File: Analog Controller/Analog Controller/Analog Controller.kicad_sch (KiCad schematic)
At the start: 12 parts, among them J1 Conn_02x06_Odd_Even, J2 Conn_02x06_Odd_Even

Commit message: Completed Analog Controller Board
Completed Analog Controller Board schematic and pcb layout :)
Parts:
- removed J1, J2: Conn_02x06_Odd_Even, symbol Connector_Generic:Conn_02x06_Odd_Even
- added C10, C11, C12, C13, C14, C15, C16, C17, C18, C4, C5, C6, C7, C8, C9: 100n, Resistor_SMD:R_0603_1608Metric_Pad0.98x0.95mm_HandSolder, symbol Device:C_Small
- added D3, D4, D5: G, LED_SMD:LED_0603_1608Metric_Pad1.05x0.95mm_HandSolder, symbol Device:LED
- added H1, H2, H3, H4: No. 8, MountingHole:MountingHole_3.2mm_M3, symbol Mechanical:MountingHole
- added J1, J4: MINIFIT-2-VERT, Connector_Molex:Molex_Mini-Fit_Jr_5566-02A_2x01_P4.20mm_Vertical, symbol BMS-Master-Revision8-eagle-import:MINIFIT-2-VERT
- added J2, J3, J8: Conn_02x08_Counter_Clockwise, Connector_PinSocket_2.54mm:PinSocket_2x08_P2.54mm_Vertical, symbol Connector_Generic:Conn_02x08_Counter_Clockwise
- added J6: MINIFIT-2-VERT, Connector_Molex:Molex_Mega-Fit_76829-0102_2x01_P5.70mm_Vertical, symbol BMS-Master-Revision8-eagle-import:MINIFIT-2-VERT
- added J7: Conn_02x09_Counter_Clockwise, Connector_Molex:Molex_Micro-Fit_3.0_43045-1812_2x09_P3.00mm_Vertical, symbol Connector_Generic:Conn_02x09_Counter_Clockwise
- added R11, R12, R13: 440, Resistor_SMD:R_0603_1608Metric_Pad0.98x0.95mm_HandSolder, symbol Device:R_US
- added R6, R7, R8: 4.7k, Resistor_SMD:R_0603_1608Metric_Pad0.98x0.95mm_HandSolder, symbol Device:R_US
- added SW1: SW_SPDT, symbol Switch:SW_SPDT
- added SW3: SW_Push_Open, symbol Switch:SW_Push_Open
- added U1, U2, U3, U6, U7, U8: TS12A12511DCNR, TS12A12511DCNR:DCN8, symbol TS12A12511DCNR:TS12A12511DCNR
- added U11, U12, U13: 74LVC1G17, Package_TO_SOT_SMD:SOT-23-5, symbol 74xGxx:74LVC1G17
- added U4: R-78C3.3-1.0, Converter_DCDC:Converter_DCDC_RECOM_R-78E-0.5_THT, symbol Regulator_Switching:R-78C3.3-1.0
- added U5: TMA-1205D, Converter_DCDC:Converter_DCDC_TRACO_TMA-05xxD_12xxD_Dual_THT, symbol Converter_DCDC:TMA-1205D
- R1, R2, R3: value R_US -> 27k; footprint (none) -> Resistor_SMD:R_0603_1608Metric_Pad0.98x0.95mm_HandSolder
- RV1, RV2, RV3: now left out of the parts list
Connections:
- net +12V: now also J2.1 (Pin_1), J2.2 (Pin_2), J3.1 (Pin_1), J3.2 (Pin_2), J6.2, J8.1 (Pin_1), J8.2 (Pin_2), U4.1 (IN), U5.1 (+Vin)
- net +3V3: now also C16.1, C17.1, C18.1, R6.1, R7.1, R8.1, U11.5 (VCC), U12.5 (VCC), U13.5 (VCC), U4.3 (OUT)
- net GND: now also C10.2, C11.2, C12.2, C13.2, C14.2, C15.2, C16.2, C17.2, C18.2, C4.2, C5.2, C6.2, C7.2, C8.2, C9.2, J1.1, J2.11 (Pin_11), J2.12 (Pin_12), J2.13 (Pin_13), J2.14 (Pin_14), J2.15 (Pin_15), J2.16 (Pin_16), J3.11 (Pin_11), J3.12 (Pin_12), J3.13 (Pin_13), J3.14 (Pin_14), J3.15 (Pin_15), J3.16 (Pin_16), J4.1, J6.1, J7.10 (Pin_10), J7.11 (Pin_11), J7.12 (Pin_12), J7.13 (Pin_13), J7.14 (Pin_14), J7.15 (Pin_15), J7.16 (Pin_16), J7.17 (Pin_17), J7.18 (Pin_18), J8.11 (Pin_11), J8.12 (Pin_12), J8.13 (Pin_13), J8.14 (Pin_14), J8.15 (Pin_15), J8.16 (Pin_16), U1.3 (GND), U11.3 (GND), U12.3 (GND), U13.3 (GND), U2.3 (GND), U3.3 (GND), U4.2 (GND), U5.2 (-Vin), U5.5 (Com), U6.3 (GND), U7.3 (GND), U8.3 (GND); no longer RV1.3, RV2.3, RV3.3
- net POT_0: now also J7.6 (Pin_6)
- net POT_1: now also J7.5 (Pin_5)
- net POT_2: now also J7.4 (Pin_4)
- new net: R13.2, U13.4
- new net: R11.2, U11.4
- new net: U7.2 (NC), U8.2 (NC)
- new net: U6.1 (COM), U7.1 (COM)
- new net: U2.1 (COM), U3.1 (COM)
- new net: U1.2 (NC), U2.2 (NC)
- new net: U3.2 (NC), U6.2 (NC)
- new net: R12.2, U12.4
- new net +5V: C10.1, C12.1, C14.1, C4.1, C6.1, C8.1, U1.4 (V+), U2.4 (V+), U3.4 (V+), U5.6 (+Vout), U6.4 (V+), U7.4 (V+), U8.4 (V+)
- new net -5V: C11.1, C13.1, C15.1, C5.1, C7.1, C9.1, U1.7 (V-), U2.7 (V-), U3.7 (V-), U5.4 (-Vout), U6.7 (V-), U7.7 (V-), U8.7 (V-)
- new net CS_0: J3.6 (Pin_6)
- new net CS_1: J3.4 (Pin_4)
- new net CS_10: J8.5 (Pin_5)
- new net CS_11: J8.3 (Pin_3)
- new net CS_2: J3.3 (Pin_3)
- new net CS_3: J3.5 (Pin_5)
- new net CS_4: J2.6 (Pin_6)
- new net CS_5: J2.4 (Pin_4)
- new net CS_6: J2.5 (Pin_5)
- new net CS_7: J2.3 (Pin_3)
- new net CS_8: J8.6 (Pin_6)
- new net CS_9: J8.4 (Pin_4)
- new net ES_0: J7.9 (Pin_9), R7.2, SW1.1 (A)
- new net ES_1: J7.8 (Pin_8), R8.2, SW1.3 (C)
- new net From_Analog_1: J3.9 (Pin_9), U2.8 (NO)
- new net From_Analog_2: J2.9 (Pin_9), U6.8 (NO)
- new net From_Analog_3: J8.9 (Pin_9), U8.8 (NO)
- new net From_Preamp: J1.2, U1.1 (COM)
- new net LED_0: U11.2
- new net LED_1: U12.2
- new net LED_2: U13.2
- new net LED_OUT_0: D3.2 (A), J7.1 (Pin_1), R11.1
- new net LED_OUT_1: D4.2 (A), J7.2 (Pin_2), R12.1
- new net LED_OUT_2: D5.2 (A), J7.3 (Pin_3), R13.1
- new net MOSI: J2.8 (Pin_8), J3.8 (Pin_8), J8.8 (Pin_8)
- new net SPDT_0: U1.6 (IN)
- new net SPDT_1: U2.6 (IN)
- new net SPDT_2: U3.6 (IN)
- new net SPDT_3: U6.6 (IN)
- new net SPDT_4: U7.6 (IN)
- new net SPDT_5: U8.6 (IN)
- new net SPI_CLK: J2.7 (Pin_7), J3.7 (Pin_7), J8.7 (Pin_7)
- new net To_Analog_1: J3.10 (Pin_10), U1.8 (NO)
- new net To_Analog_2: J2.10 (Pin_10), U3.8 (NO)
- new net To_Analog_3: J8.10 (Pin_10), U7.8 (NO)
- new net To_Dig_Board: J4.2, U8.1 (COM)
- new net Toggle_ON/OFF: J7.7 (Pin_7), R6.2, SW3.1 (A)
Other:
- sheet STM32_MCU ports: added CS_10, CS_11, CS_9, Effect_Select_0, Effect_Select_1, LED_0, LED_1, LED_2, SPDT_IO_0, SPDT_IO_1, SPDT_IO_2, SPDT_IO_3, SPDT_IO_4, SPDT_IO_5, Toggle_ON/OFF; removed MISO
- note added: "For Pot: Potentiometer = 0 ohm - 10k ohm When pot is 0 ohms, ADC reads 0V When pot is 10k ohms, ADC reads 3.2V"
- note added: "For SPDT: Reads 0V or 3V3"
- note added: "Power"
- note added: "Schmitt Trigger"
- moved on the sheet: D1, D2, R1, R2, R3, R4, R5, RV1, RV2, RV3

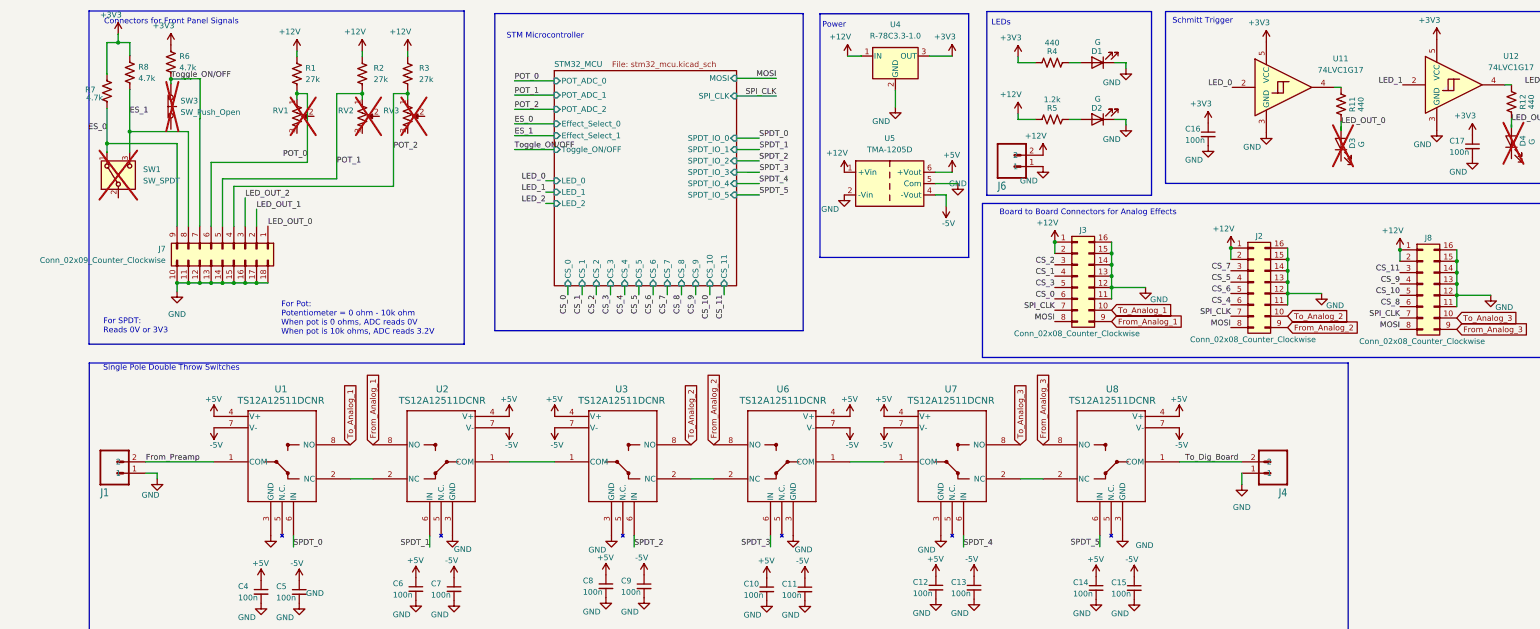
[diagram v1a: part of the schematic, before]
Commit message: Added new stm32 microcontroller, redid pcb layout
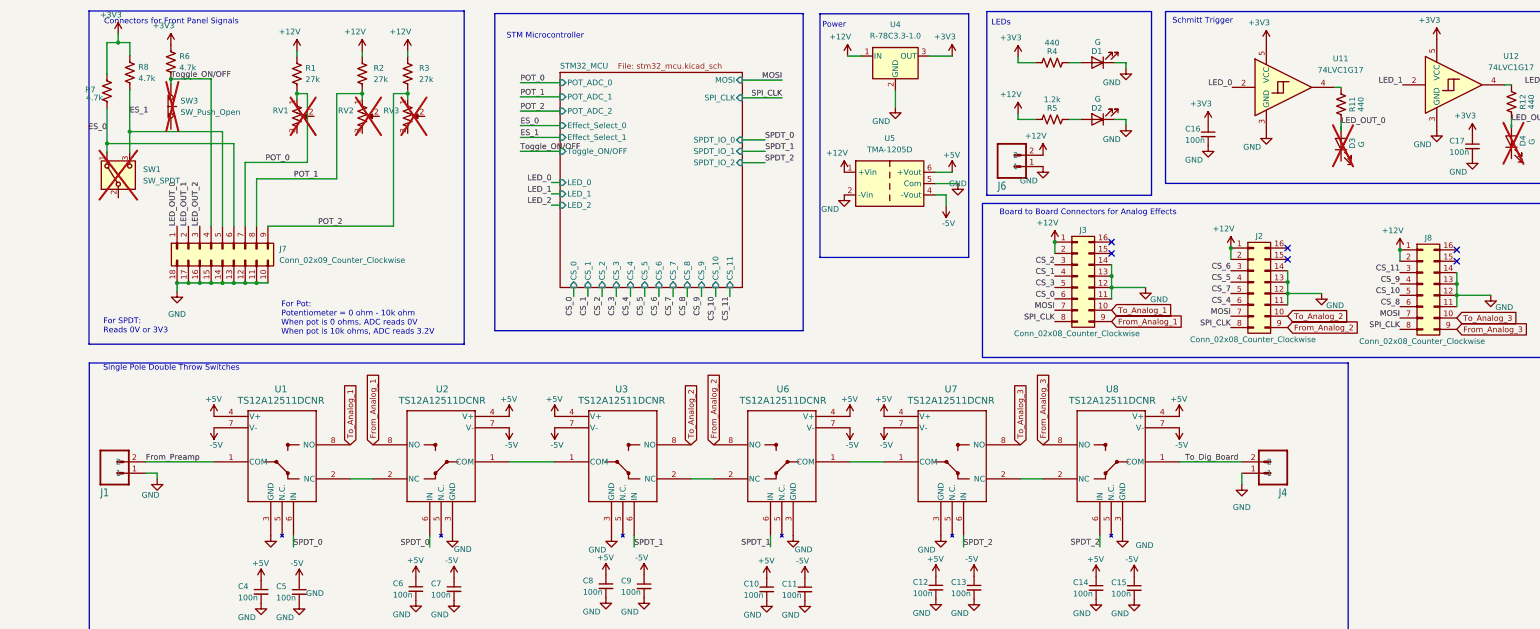
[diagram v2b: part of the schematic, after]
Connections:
- net SPDT_3 is gone; now on net SPDT_1: U6.6 (IN)
- net SPDT_4 is gone; now on net SPDT_2: U7.6 (IN)
- net SPDT_5 is gone; now on net SPDT_2: U8.6 (IN)
- net CS_6: now also J2.3 (Pin_3); no longer J2.5 (Pin_5)
- net CS_7: now also J2.5 (Pin_5); no longer J2.3 (Pin_3)
- net ES_0: now also J7.6 (Pin_6); no longer J7.9 (Pin_9)
- net ES_1: now also J7.5 (Pin_5); no longer J7.8 (Pin_8)
- net GND: no longer J2.15 (Pin_15), J2.16 (Pin_16), J3.15 (Pin_15), J3.16 (Pin_16), J8.15 (Pin_15), J8.16 (Pin_16)
- net MOSI: now also J2.7 (Pin_7), J3.7 (Pin_7), J8.7 (Pin_7); no longer J2.8 (Pin_8), J3.8 (Pin_8), J8.8 (Pin_8)
- net POT_0: now also J7.7 (Pin_7); no longer J7.6 (Pin_6)
- net POT_1: now also J7.8 (Pin_8); no longer J7.5 (Pin_5)
- net POT_2: now also J7.9 (Pin_9); no longer J7.4 (Pin_4)
- net SPDT_0: now also U2.6 (IN)
- net SPDT_1: now also U3.6 (IN); no longer U2.6 (IN)
- net SPDT_2: no longer U3.6 (IN)
- net SPI_CLK: now also J2.8 (Pin_8), J3.8 (Pin_8), J8.8 (Pin_8); no longer J2.7 (Pin_7), J3.7 (Pin_7), J8.7 (Pin_7)
- net Toggle_ON/OFF: now also J7.4 (Pin_4); no longer J7.7 (Pin_7)
- no-connect marks 0 -> 6
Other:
- sheet STM32_MCU ports: added none; removed SPDT_IO_3, SPDT_IO_4, SPDT_IO_5
- moved on the sheet: J7

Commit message: Incorporated changes from demo
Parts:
- added C1: 0.1u, Resistor_SMD:R_0603_1608Metric_Pad0.98x0.95mm_HandSolder, symbol Device:C_Small
- added R9: 240, Resistor_SMD:R_0603_1608Metric_Pad0.98x0.95mm_HandSolder, symbol Device:R_US
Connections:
- net GND: now also C1.2
- net To_Dig_Board: now also C1.1, R9.1; no longer U8.1 (COM)
- new net: R9.2, U8.1 (COM)
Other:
- moved on the sheet: J4

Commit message: fixes for Marco's dr
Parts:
- added C2: 1u, Capacitor_SMD:C_0603_1608Metric, symbol Device:C
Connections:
- net From_Preamp: now also C2.1; no longer U1.1 (COM)
- new net: C2.2, U1.1 (COM)
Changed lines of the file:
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@@
 	(wire
 		(pts
+			(xy 43.18 123.19) (xy 48.26 123.19)
+		)
+		(stroke
+			(width 0)
+			(type default)
+		)
+	)
+	(wire
+		(pts
 			(xy 259.1664 81.6582) (xy 259.1664 84.1982)
 		)
@@
 	(wire
 		(pts
-			(xy 43.18 123.19) (xy 58.42 123.19)
-		)
-		(stroke
-			(width 0)
-			(type default)
-		)
-	)
-	(wire
-		(pts
 			(xy 53.1827 37.5174) (xy 57.785 37.5174)
 		)
@@
 	(wire
 		(pts
+			(xy 55.88 123.19) (xy 58.42 123.19)
+		)
+		(stroke
+			(width 0)
+			(type default)
+		)
+	)
+	(wire
+		(pts
 			(xy 51.9127 37.5694) (xy 48.7893 37.5694)
 		)
@@
 	)
 	(label "From_Preamp"
-		(at 43.18 123.19 0)
+		(at 43.18 123.19 90)
 		(effects
 			(font
@@
 					(unit 1)
 				)
+			)
+		)
+	)
+	(symbol
+		(lib_id "Device:C")
+		(at 52.07 123.19 90)
+		(unit 1)
+		(exclude_from_sim no)
+		(in_bom yes)
+		(on_board yes)
+		(dnp no)
+		(fields_autoplaced yes)
+		(property "Reference" "C2"
+			(at 52.07 115.57 90)
+			(effects
+				(font
+					(size 1.27 1.27)
+				)
+			)
+		)
+		(property "Value" "1u"
+			(at 52.07 118.11 90)
+			(effects
+				(font
+					(size 1.27 1.27)
+				)
+			)
+		)
+		(property "Footprint" "Capacitor_SMD:C_0603_1608Metric"
+			(at 55.88 122.2248 0)
+			(effects
+				(font
+					(size 1.27 1.27)
+				)
+				(hide yes)
+			)
+		)
+		(property "Datasheet" "~"
+			(at 52.07 123.19 0)
+			(effects
+				(font
+					(size 1.27 1.27)
+				)
+				(hide yes)
+			)
+		)
+		(property "Description" "Unpolarized capacitor"
+			(at 52.07 123.19 0)
+			(effects
+				(font
+					(size 1.27 1.27)
+				)
+				(hide yes)
+			)
+		)
+		(pin "1"
+		)
+		(pin "2"
+		)
+		(instances
+			(project ""
+				(path "/1bac89ce-58dc-4152-afeb-ef1b4a92587d"
+					(reference "C2")
+					(unit 1)
+				)
